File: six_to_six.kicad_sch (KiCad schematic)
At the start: 0 parts

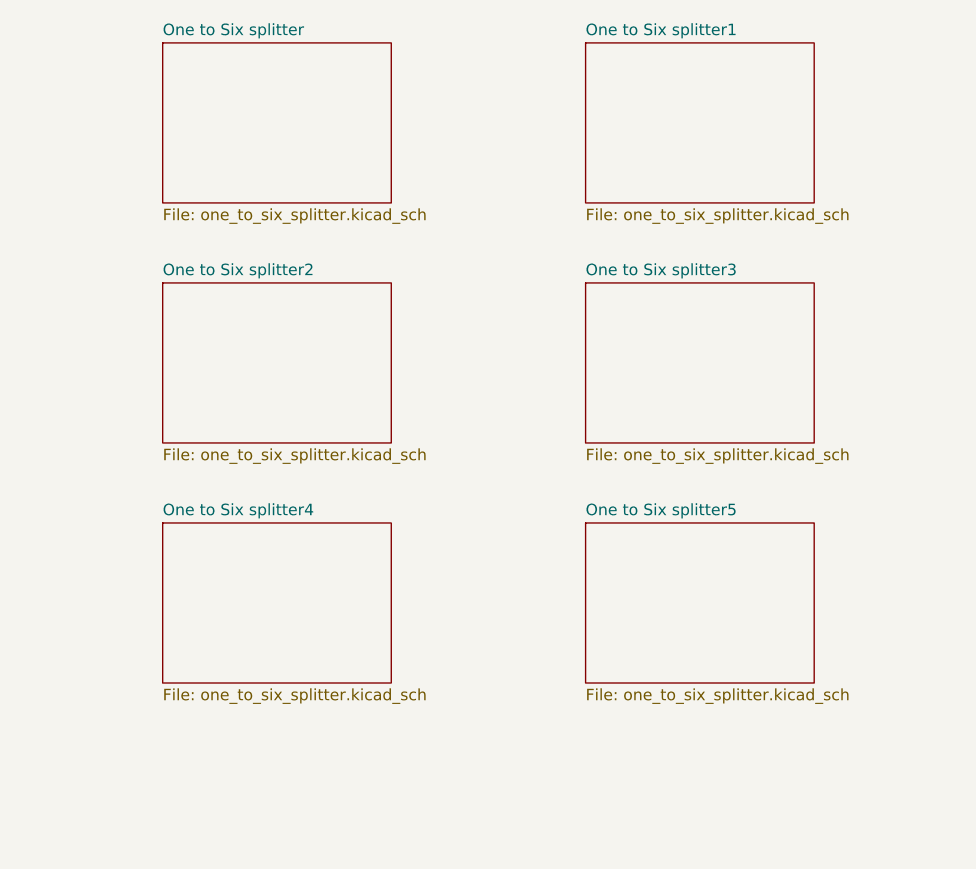
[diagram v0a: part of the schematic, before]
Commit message: changed to 1 to 6
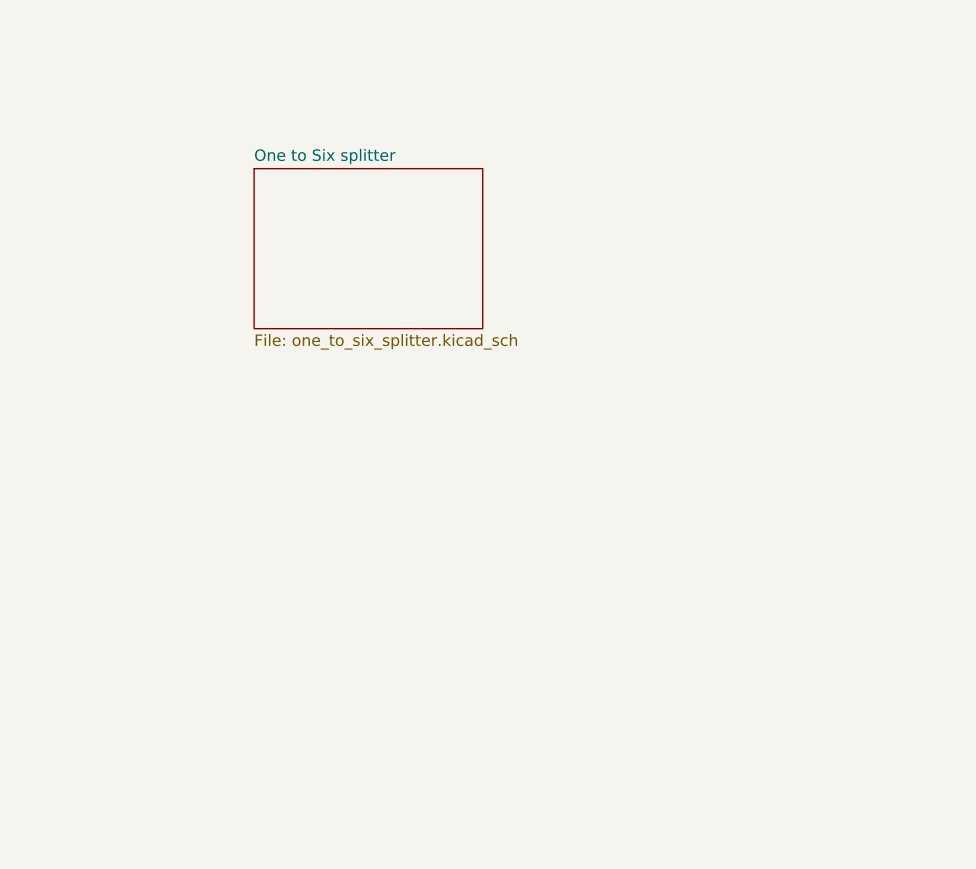
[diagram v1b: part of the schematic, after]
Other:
- removed sheet One to Six splitter1
- removed sheet One to Six splitter2
- removed sheet One to Six splitter3
- removed sheet One to Six splitter4
- removed sheet One to Six splitter5

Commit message: pcb routed and made gerbers
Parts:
- added H1, H2, H3: M3, MountingHole:MountingHole_3.2mm_M3_DIN965_Pad, symbol Mechanical:MountingHole_Pad
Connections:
- net GND: now also H1.1, H2.1, H3.1

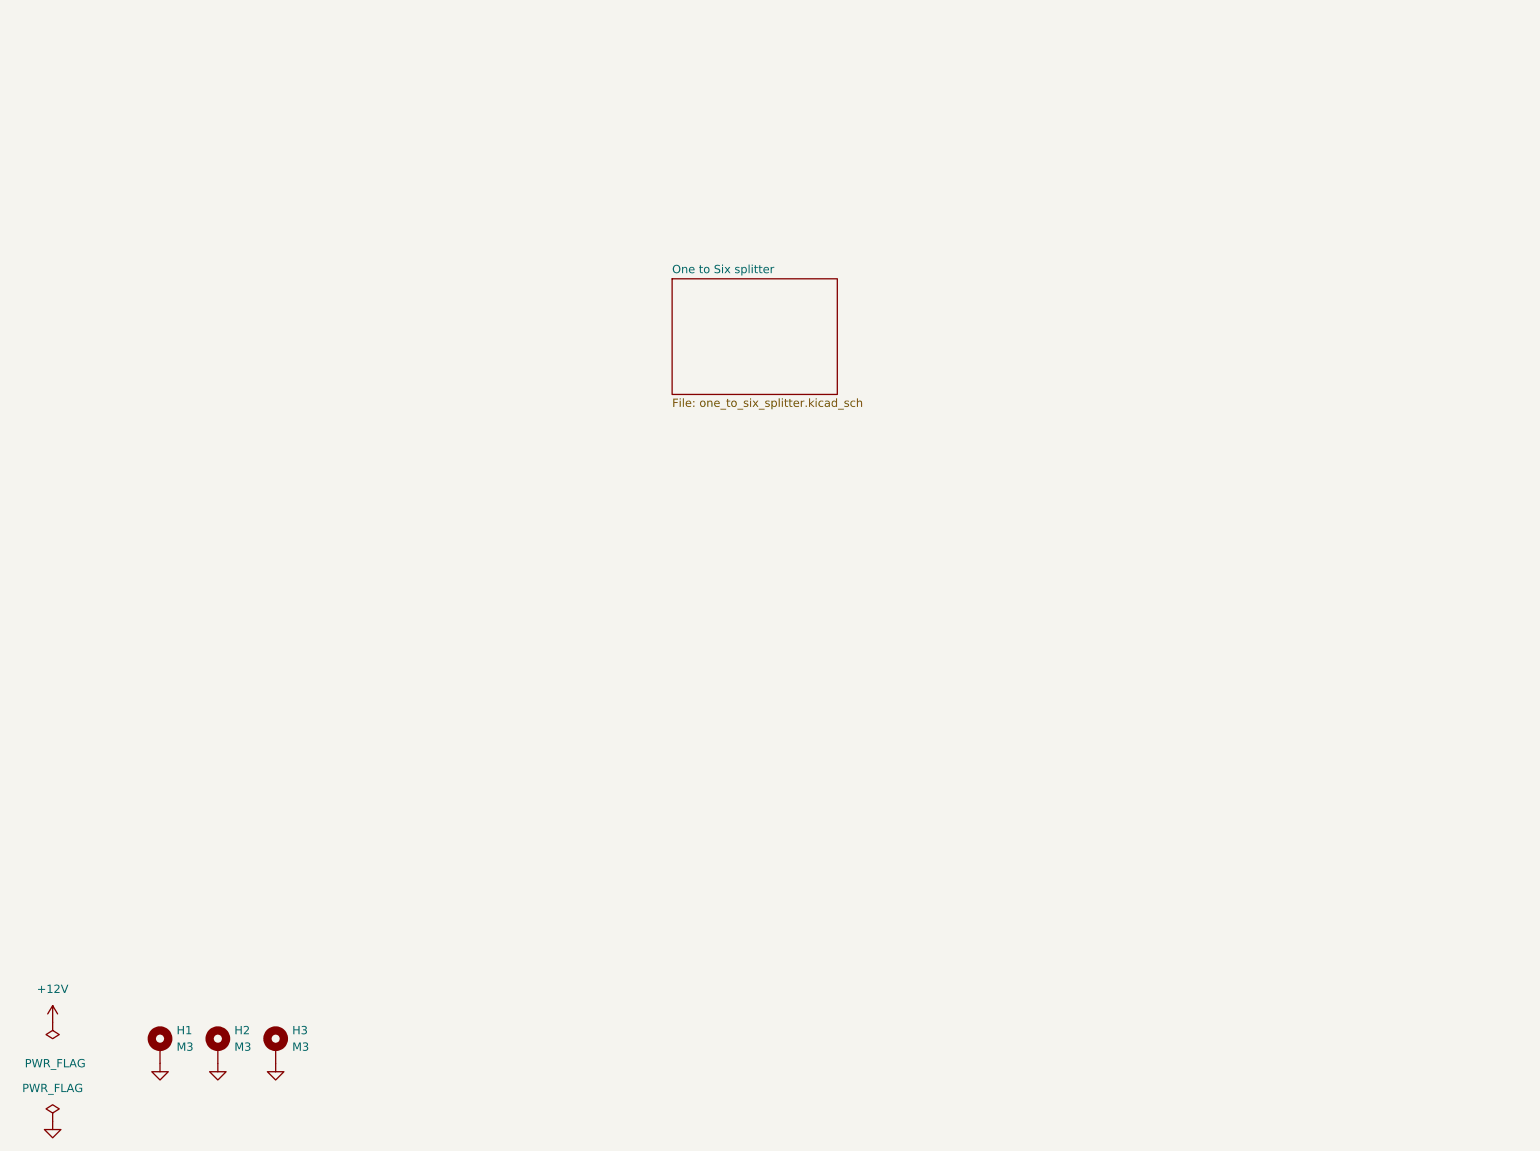
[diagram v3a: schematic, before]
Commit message: changed footprint for 2-way splitter transformer
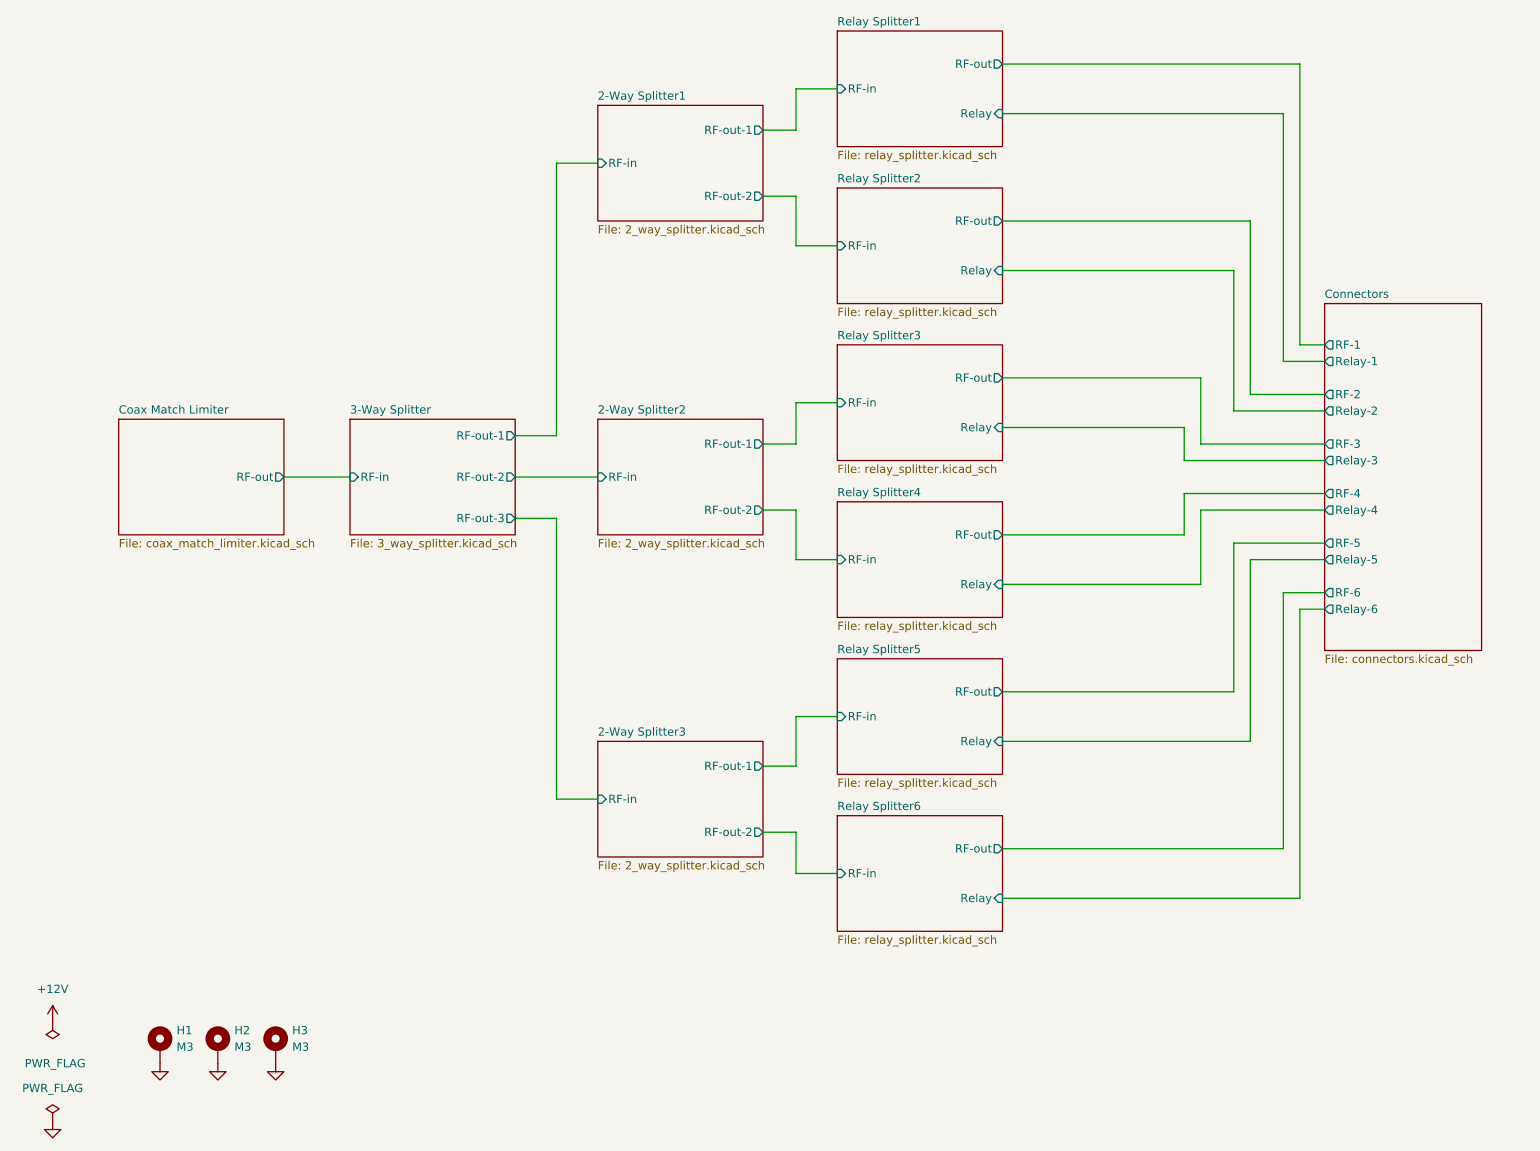
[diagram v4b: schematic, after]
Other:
- removed sheet One to Six splitter
- added sheet 2-Way Splitter1 (2_way_splitter.kicad_sch)
- added sheet 2-Way Splitter2 (2_way_splitter.kicad_sch)
- added sheet 2-Way Splitter3 (2_way_splitter.kicad_sch)
- added sheet 3-Way Splitter (3_way_splitter.kicad_sch)
- added sheet Coax Match Limiter (coax_match_limiter.kicad_sch)
- added sheet Connectors (connectors.kicad_sch)
- added sheet Relay Splitter1 (relay_splitter.kicad_sch)
- added sheet Relay Splitter2 (relay_splitter.kicad_sch)
- added sheet Relay Splitter3 (relay_splitter.kicad_sch)
- added sheet Relay Splitter4 (relay_splitter.kicad_sch)
- added sheet Relay Splitter5 (relay_splitter.kicad_sch)
- added sheet Relay Splitter6 (relay_splitter.kicad_sch)

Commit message: move mounting hole mere inside
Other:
- company: S59MZ -> S55O, S59MZ
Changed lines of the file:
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@@
     (date "2023-02-18")
     (rev "1.0")
-    (company "S59MZ")
+    (company "S55O, S59MZ")
   )
   (wire (pts (xy 213.36 81.28) (xy 201.93 81.28))
